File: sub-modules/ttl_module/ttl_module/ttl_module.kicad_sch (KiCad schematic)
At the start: 1 part, among them J1 Conn_02x06_Odd_Even

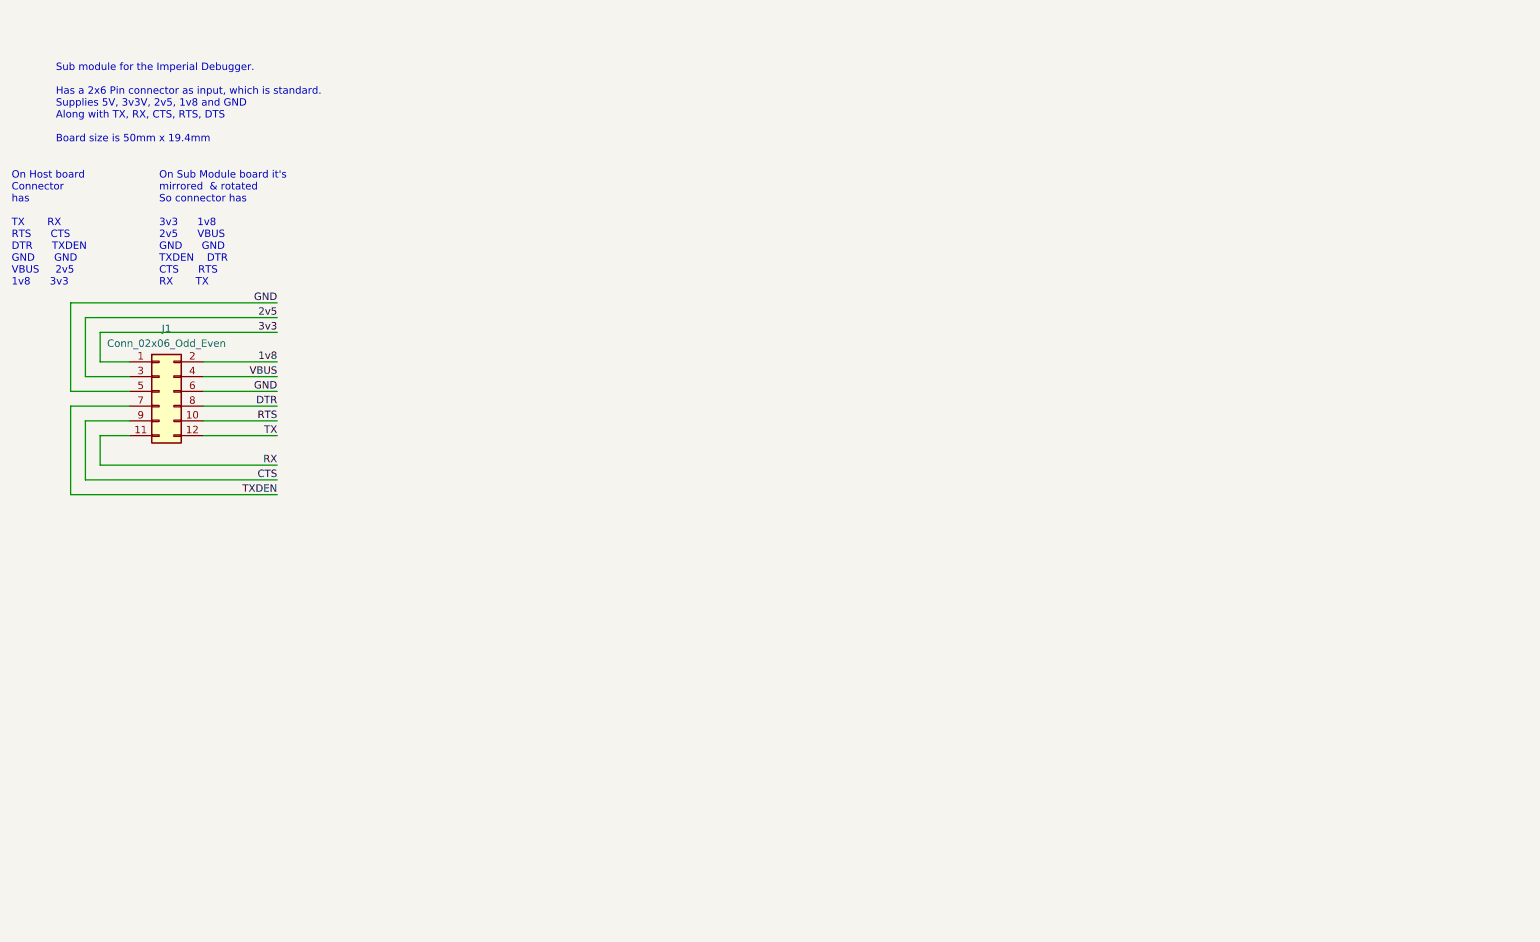
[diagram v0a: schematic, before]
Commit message: Updated Schematic and PCB for first pass at the design
Signed-off-by: Marc Kelly <mpkelly@achenar.co.uk>
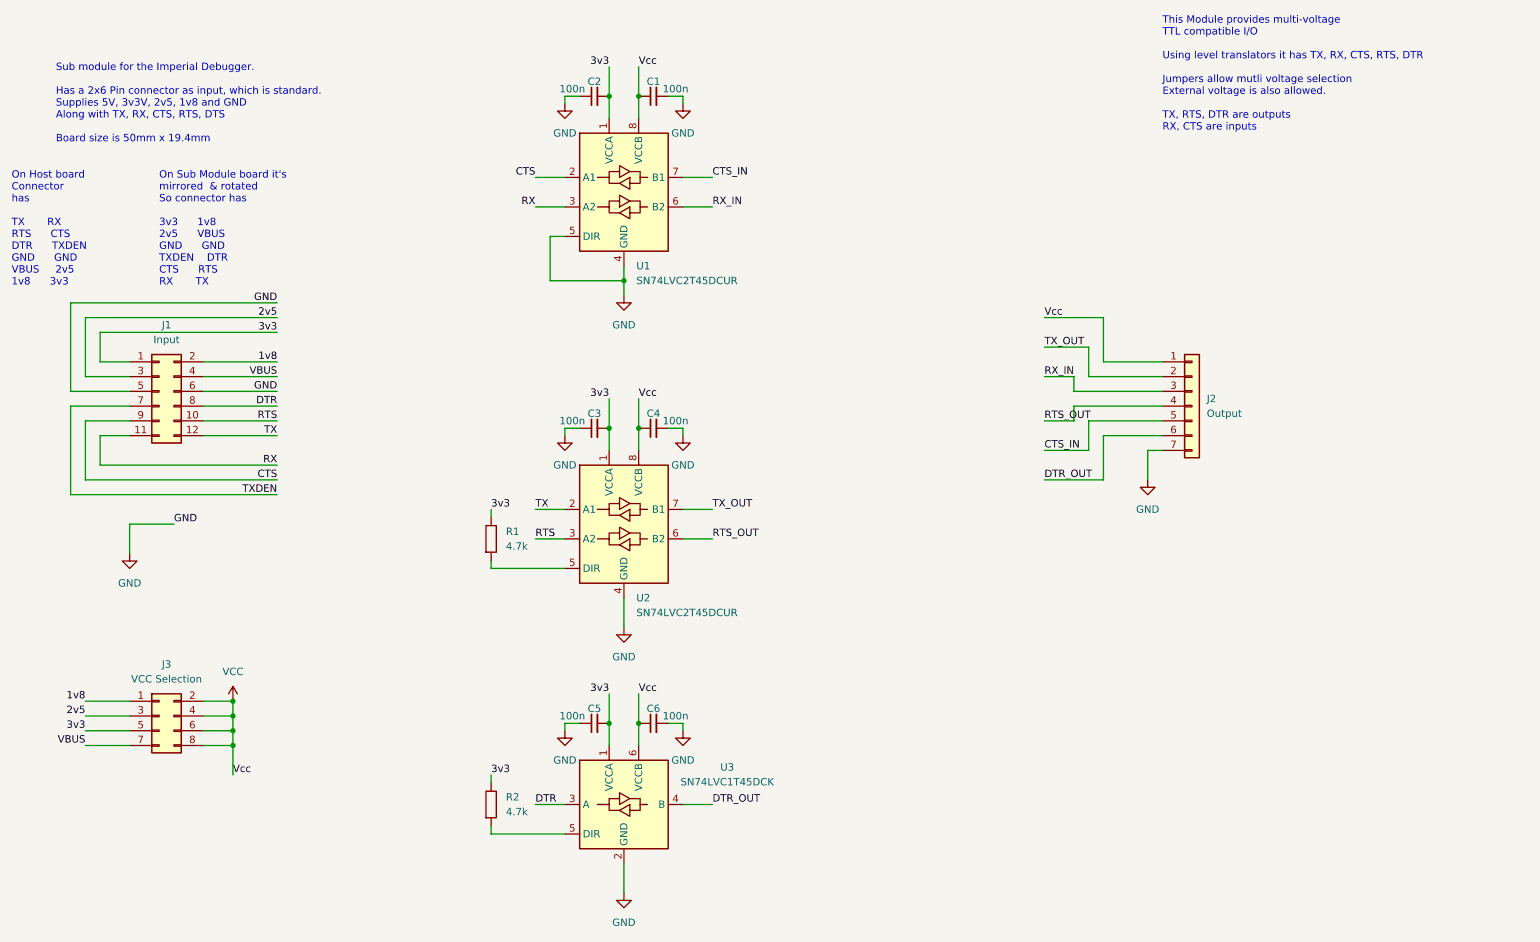
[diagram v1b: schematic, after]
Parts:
- added C1, C2, C3, C4, C5, C6: 100n, Capacitor_SMD:C_0603_1608Metric_Pad1.08x0.95mm_HandSolder, symbol Device:C_Small
- added J2: Output, Connector_PinHeader_2.54mm:PinHeader_1x07_P2.54mm_Vertical, symbol Connector_Generic:Conn_01x07
- added J3: VCC Selection, Connector_PinHeader_2.54mm:PinHeader_2x04_P2.54mm_Vertical, symbol Connector_Generic:Conn_02x04_Odd_Even
- added R1, R2: 4.7k, Resistor_SMD:R_0603_1608Metric_Pad0.98x0.95mm_HandSolder, symbol PCM_SL_Resistors:4.7k
- added U1, U2: SN74LVC2T45DCUR, Package_SO:VSSOP-8_2.3x2mm_P0.5mm, symbol Logic_LevelTranslator:SN74LVC2T45DCUR
- added U3: SN74LVC1T45DCK, Package_TO_SOT_SMD:SOT-363_SC-70-6, symbol Logic_LevelTranslator:SN74LVC1T45DCK
- J1: value Conn_02x06_Odd_Even -> Input
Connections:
- net 1v8: now also J3.1 (Pin_1)
- net 2v5: now also J3.3 (Pin_3)
- net 3v3: now also C2.2, C3.2, C5.2, J3.5 (Pin_5), R1.2, R2.2, U1.1 (VCCA), U2.1 (VCCA), U3.1 (VCCA)
- net CTS: now also U1.2 (A1)
- net DTR: now also U3.3 (A)
- net GND: now also C1.2, C2.1, C3.1, C4.2, C5.1, C6.2, J2.7 (Pin_7), U1.4 (GND), U1.5 (DIR), U2.4 (GND), U3.2 (GND)
- net RTS: now also U2.3 (A2)
- net RX: now also U1.3 (A2)
- net TX: now also U2.2 (A1)
- net VBUS: now also J3.7 (Pin_7)
- new net: R2.1, U3.5 (DIR)
- new net: R1.1, U2.5 (DIR)
- new net CTS_IN: J2.5 (Pin_5), U1.7 (B1)
- new net DTR_OUT: J2.6 (Pin_6), U3.4 (B)
- new net RTS_OUT: J2.4 (Pin_4), U2.6 (B2)
- new net RX_IN: J2.3 (Pin_3), U1.6 (B2)
- new net TX_OUT: J2.2 (Pin_2), U2.7 (B1)
- new net VCC: C1.1, C4.1, C6.1, J2.1 (Pin_1), J3.2 (Pin_2), J3.4 (Pin_4), J3.6 (Pin_6), J3.8 (Pin_8), U1.8 (VCCB), U2.8 (VCCB), U3.6 (VCCB)
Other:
- note added: "This Module provides multi-voltage TTL compatible I/O Using level translators it has TX, RX, CTS, RTS, DTR Jumpers allow mutli voltage selection External voltage is also allowed. TX, RTS, DTR are outputs RX, CTS are inputs"

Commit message: Update schematics after moving to KiCad 10
Added some footprints to a local lib, as the silkscreen caused issues.

Signed-off-by: Marc Kelly <mpkelly@achenar.co.uk>
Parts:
- J1: footprint Connector_PinSocket_2.54mm:PinSocket_2x06_P2.54mm_Horizontal -> Local:PinSocket_2x06_P2.54mm_Horizontal

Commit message: Sorting out BOMs
Signed-off-by: Marc Kelly <mpkelly@achenar.co.uk>
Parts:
- C1, C2, C3, C4, C5, C6: MFN (none) -> Generic X7R; MFP (none) -> 100nF; SUPPLIER (none) -> Mouser; SUPPLIER_PN (none) -> 581-06035C104JAT2A62
- J1: MFN (none) -> Wurth; MFP (none) -> 613012243121; SUPPLIER (none) -> Mouser; SUPPLIER_PN (none) -> 710-613012243121
- J2: MFN (none) -> Harwin; MFP (none) -> M20-9990745; SUPPLIER (none) -> Mouser; SUPPLIER_PN (none) -> 855-M20-9990745
- J3: MFN (none) -> Harwin; MFP (none) -> M20-9760442; SUPPLIER (none) -> Mouser; SUPPLIER_PN (none) -> 855-M20-9760442
- R1, R2: MFN (none) -> Generic; MFP (none) -> 4.7k 1%; SUPPLIER (none) -> Mouser; SUPPLIER_PN (none) -> 594-MCT06030C4701FP5
- U1, U2: value SN74LVC2T45DCUR -> SN74LVC2T45DCTR; footprint Package_SO:VSSOP-8_2.3x2mm_P0.5mm -> Snapeda:SOP65P400X130-8N; symbol Logic_LevelTranslator:SN74LVC2T45DCUR -> Snapeda:SN74LVC2T45DCTR; MFN (none) -> Texas Instruments; MFP (none) -> SN74LVC2T45DCTR; SUPPLIER (none) -> Mouser; SUPPLIER_PN (none) -> 595-SN74LVC2T45DCTR
- U3: MFN (none) -> Texas Instruments; MFP (none) -> SN74LVC1T45DCKR; SUPPLIER (none) -> Mouser; SUPPLIER_PN (none) -> 595-SN74LVC1T45DCKR
